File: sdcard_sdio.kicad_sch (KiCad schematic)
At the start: 13 parts, among them J7 SD_Card, U11 MIC2025-2YM

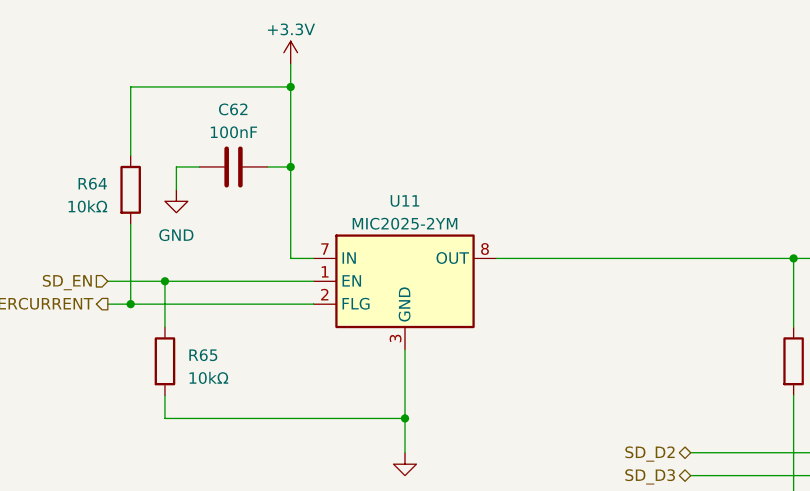
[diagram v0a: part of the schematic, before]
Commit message: Corrected part number for the SD Card load switch
The MIC2025-2 is active low so the pull-down enables it by default
(not what was intended) the MIC2025-1 is active high input and is
what this circuit was designed for.
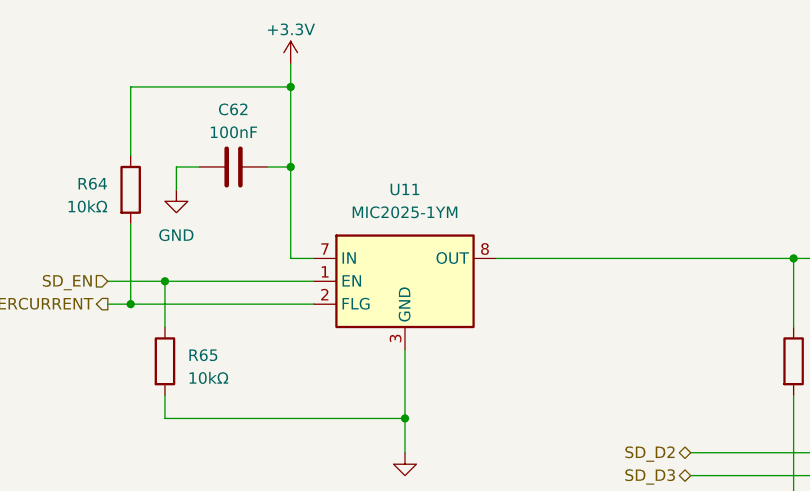
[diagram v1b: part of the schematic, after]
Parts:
- U11: value MIC2025-2YM -> MIC2025-1YM
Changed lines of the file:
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@@
   (symbol (lib_id "Power_Management:MIC2025-2YM") (at 81.28 71.12 0) (unit 1)
     (in_bom yes) (on_board yes) (dnp no) (fields_autoplaced)
-    (property "Reference" "U11" (at 81.28 62.23 0)
+    (property "Reference" "U11" (at 81.28 60.96 0)
       (effects (font (size 1.27 1.27)))
     )
-    (property "Value" "MIC2025-2YM" (at 81.28 64.77 0)
+    (property "Value" "MIC2025-1YM" (at 81.28 63.5 0)
       (effects (font (size 1.27 1.27)))
     )
